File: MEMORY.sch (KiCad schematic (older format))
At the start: 77 parts, among them J901 GND, J902 GND, J903 GND, J904 GND, J905 GND, J906 GND, J907 GND, J908 GND, J909 GND, J910 GND, J911 GND, J912 GND, J913 GND, J914 GND, J915 GND, J916 GND, J917 GND, J918 GND, J919 GND, J920 GND, J921 GND, J922 GND, J923 GND, J924 GND, U801 MCIMX7D7DVM10SC, U901 MT41K256M16HA-125, U902 MT41K256M16HA-125

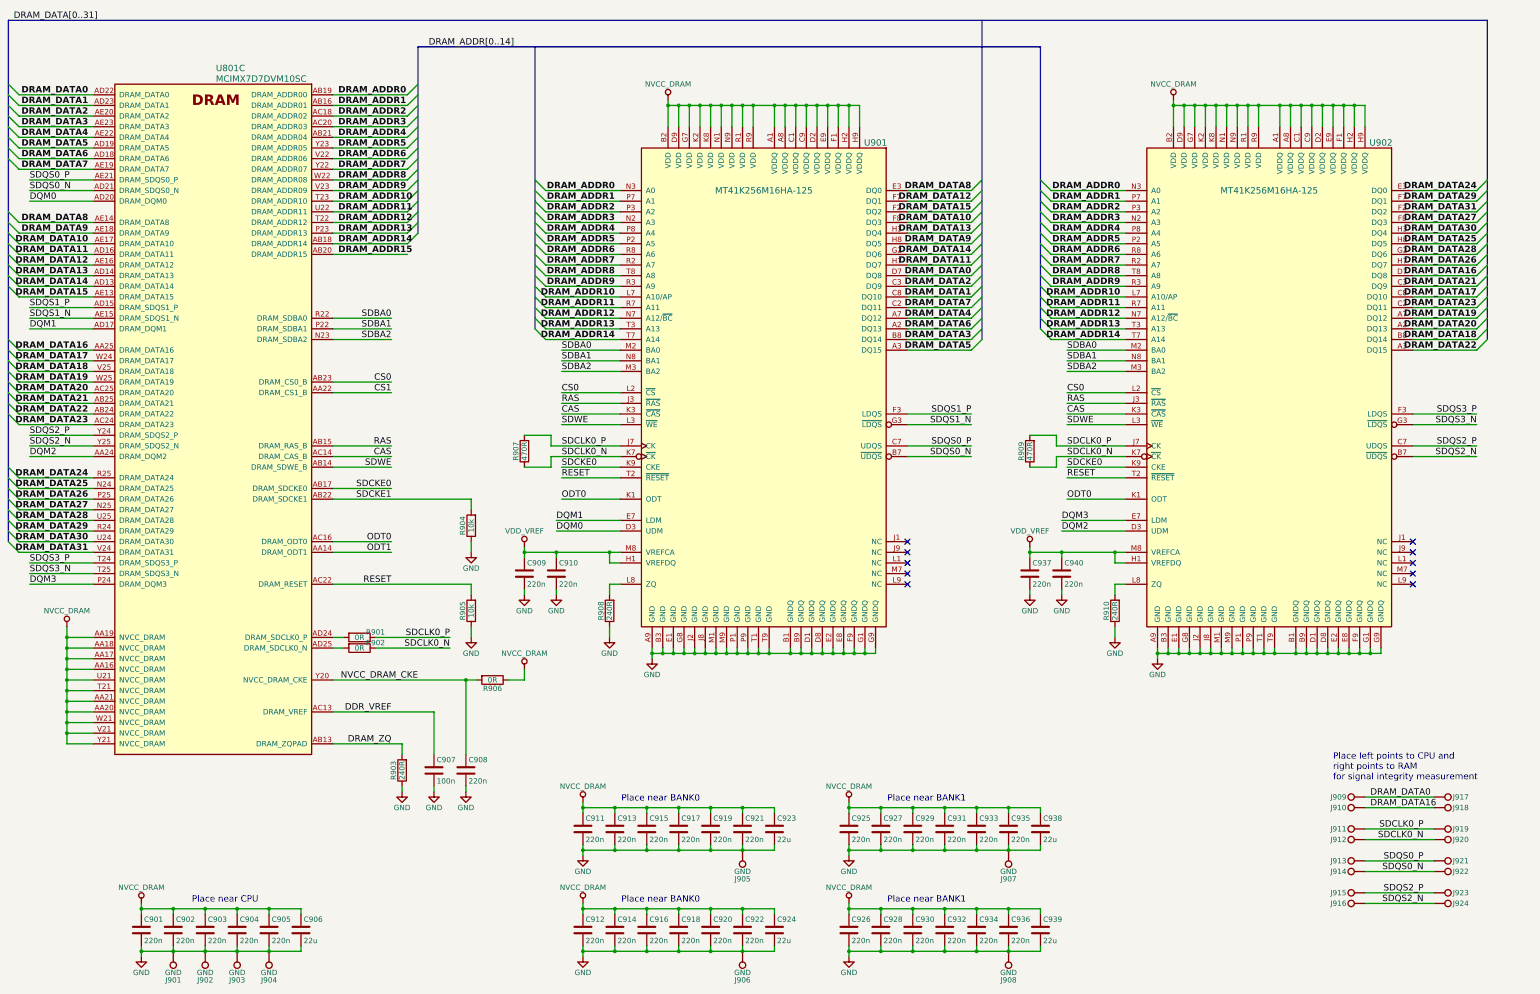
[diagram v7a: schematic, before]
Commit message: This branch moves from i.mx7 to STM32F4 CPU to be finished for Hackaday Prize 2017
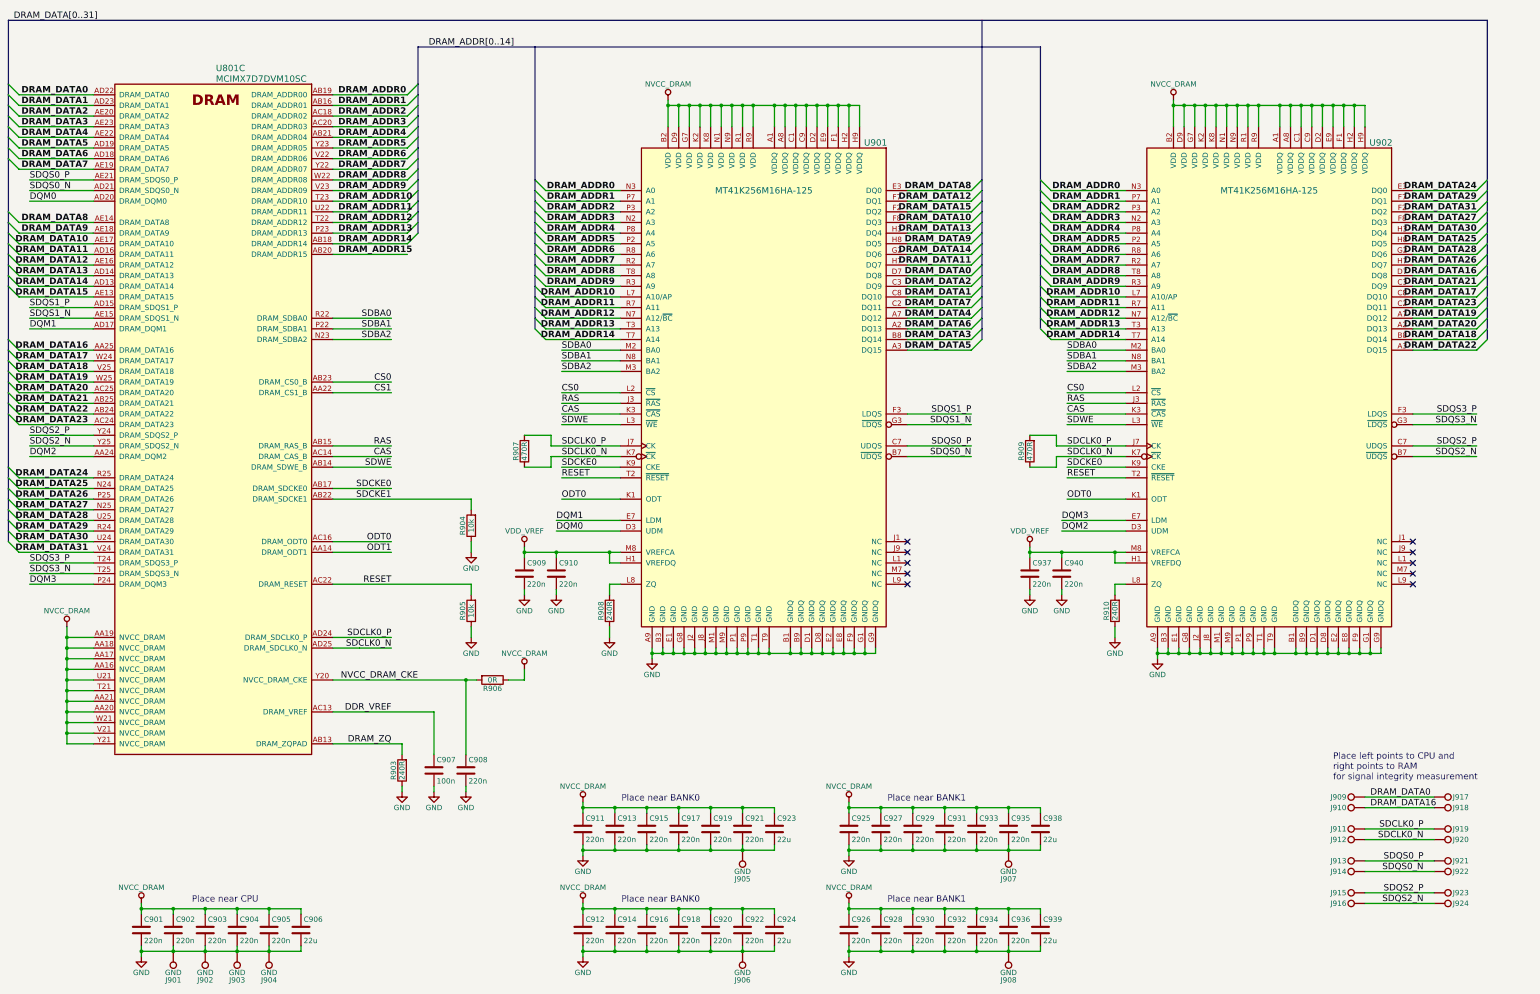
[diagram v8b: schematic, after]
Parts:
- removed R901, R902: 0R, Resistors_SMD:R_0402, symbol R
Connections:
- net SDCLK0_N: now also U801.AD25 (DRAM_SDCLK0_N)
- net SDCLK0_P: now also U801.AD24 (DRAM_SDCLK0_P)
